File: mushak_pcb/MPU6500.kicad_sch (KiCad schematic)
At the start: 9 parts, among them U5 MPU-6500

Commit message: Add footprints
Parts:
- C31, C32, C33: footprint (none) -> Capacitor_SMD:C_0805_2012Metric
- R16, R17, R18, R19, R20: footprint (none) -> Resistor_SMD:R_0805_2012Metric
- U5: footprint QFN40P300X300X95-25N -> MPU-6500:QFN40P300X300X95-25N
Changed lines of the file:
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@@
     (property "Reference" "R19" (id 0) (at 133.858 54.61 90))
     (property "Value" "10k" (id 1) (at 133.858 57.15 90))
-    (property "Footprint" "" (id 2) (at 133.858 62.484 90)
+    (property "Footprint" "Resistor_SMD:R_0805_2012Metric" (id 2) (at 133.858 62.484 90)
       (effects (font (size 1.27 1.27)) hide)
     )
@@
       (effects (font (size 1.27 1.27)) (justify left))
     )
-    (property "Footprint" "" (id 2) (at 125.73 101.854 90)
+    (property "Footprint" "Resistor_SMD:R_0805_2012Metric" (id 2) (at 125.73 101.854 90)
       (effects (font (size 1.27 1.27)) hide)
     )
@@
     (property "Reference" "R20" (id 0) (at 168.91 85.09 90))
     (property "Value" "10k" (id 1) (at 171.958 82.804 90))
-    (property "Footprint" "" (id 2) (at 171.958 84.582 90)
+    (property "Footprint" "Resistor_SMD:R_0805_2012Metric" (id 2) (at 171.958 84.582 90)
       (effects (font (size 1.27 1.27)) hide)
     )
@@
       (effects (font (size 1.27 1.27)) (justify left))
     )
-    (property "Footprint" "" (id 2) (at 179.2732 54.102 0)
+    (property "Footprint" "Capacitor_SMD:C_0805_2012Metric" (id 2) (at 179.2732 54.102 0)
       (effects (font (size 1.27 1.27)) hide)
     )
@@
       (effects (font (size 1.27 1.27)) (justify left))
     )
-    (property "Footprint" "" (id 2) (at 169.3672 54.102 0)
+    (property "Footprint" "Capacitor_SMD:C_0805_2012Metric" (id 2) (at 169.3672 54.102 0)
       (effects (font (size 1.27 1.27)) hide)
     )
@@
     (property "Reference" "U5" (id 0) (at 148.082 64.77 0))
     (property "Value" "MPU-6500" (id 1) (at 148.082 67.31 0))
-    (property "Footprint" "QFN40P300X300X95-25N" (id 2) (at 148.082 87.884 0)
+    (property "Footprint" "MPU-6500:QFN40P300X300X95-25N" (id 2) (at 148.082 87.884 0)
       (effects (font (size 1.27 1.27)) (justify left bottom) hide)
     )
@@
       (effects (font (size 1.27 1.27)) (justify right))
     )
-    (property "Footprint" "" (id 2) (at 114.3 69.088 90)
+    (property "Footprint" "Resistor_SMD:R_0805_2012Metric" (id 2) (at 114.3 69.088 90)
       (effects (font (size 1.27 1.27)) hide)
     )
@@
     (property "Reference" "C32" (id 0) (at 169.418 88.646 90))
     (property "Value" "0.1uF" (id 1) (at 176.276 88.9 90))
-    (property "Footprint" "" (id 2) (at 168.148 91.3892 0)
+    (property "Footprint" "Capacitor_SMD:C_0805_2012Metric" (id 2) (at 168.148 91.3892 0)
       (effects (font (size 1.27 1.27)) hide)
     )
@@
       (effects (font (size 1.27 1.27)) (justify right))
     )
-    (property "Footprint" "" (id 2) (at 122.428 68.834 90)
-      (effects (font (size 1.27 1.27)) hide)
-    )
+    (property "Footprint" "Resistor_SMD:R_0805_2012Metric" (id 2) (at 122.428 68.834 90)
+      (effects (font (size 1.27 1.27)) hide)
+    )

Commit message: Update Schematics and footprints for sensors
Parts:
- C31, C32, C33: footprint Capacitor_SMD:C_0805_2012Metric -> Capacitor_SMD:C_0402_1005Metric
- R16, R17, R18, R19, R20: footprint Resistor_SMD:R_0805_2012Metric -> Resistor_SMD:R_0402_1005Metric
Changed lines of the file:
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@@
     (property "Reference" "R19" (id 0) (at 133.858 54.61 90))
     (property "Value" "10k" (id 1) (at 133.858 57.15 90))
-    (property "Footprint" "Resistor_SMD:R_0805_2012Metric" (id 2) (at 133.858 62.484 90)
+    (property "Footprint" "Resistor_SMD:R_0402_1005Metric" (id 2) (at 133.858 62.484 90)
       (effects (font (size 1.27 1.27)) hide)
     )
@@
       (effects (font (size 1.27 1.27)) (justify left))
     )
-    (property "Footprint" "Resistor_SMD:R_0805_2012Metric" (id 2) (at 125.73 101.854 90)
+    (property "Footprint" "Resistor_SMD:R_0402_1005Metric" (id 2) (at 125.73 101.854 90)
       (effects (font (size 1.27 1.27)) hide)
     )
@@
     (property "Reference" "R20" (id 0) (at 168.91 85.09 90))
     (property "Value" "10k" (id 1) (at 171.958 82.804 90))
-    (property "Footprint" "Resistor_SMD:R_0805_2012Metric" (id 2) (at 171.958 84.582 90)
+    (property "Footprint" "Resistor_SMD:R_0402_1005Metric" (id 2) (at 171.958 84.582 90)
       (effects (font (size 1.27 1.27)) hide)
     )
@@
       (effects (font (size 1.27 1.27)) (justify left))
     )
-    (property "Footprint" "Capacitor_SMD:C_0805_2012Metric" (id 2) (at 179.2732 54.102 0)
+    (property "Footprint" "Capacitor_SMD:C_0402_1005Metric" (id 2) (at 179.2732 54.102 0)
       (effects (font (size 1.27 1.27)) hide)
     )
@@
       (effects (font (size 1.27 1.27)) (justify left))
     )
-    (property "Footprint" "Capacitor_SMD:C_0805_2012Metric" (id 2) (at 169.3672 54.102 0)
+    (property "Footprint" "Capacitor_SMD:C_0402_1005Metric" (id 2) (at 169.3672 54.102 0)
       (effects (font (size 1.27 1.27)) hide)
     )
@@
       (effects (font (size 1.27 1.27)) (justify left bottom) hide)
     )
-    (property "Datasheet" "" (id 3) (at 148.082 87.884 0)
+    (property "Datasheet" "https://invensense.tdk.com/wp-content/uploads/2020/06/PS-MPU-6500A-01-v1.3.pdf" (id 3) (at 148.082 87.884 0)
       (effects (font (size 1.27 1.27)) (justify left bottom) hide)
     )
@@
       (effects (font (size 1.27 1.27)) (justify right))
     )
-    (property "Footprint" "Resistor_SMD:R_0805_2012Metric" (id 2) (at 114.3 69.088 90)
+    (property "Footprint" "Resistor_SMD:R_0402_1005Metric" (id 2) (at 114.3 69.088 90)
       (effects (font (size 1.27 1.27)) hide)
     )
@@
     (property "Reference" "C32" (id 0) (at 169.418 88.646 90))
     (property "Value" "0.1uF" (id 1) (at 176.276 88.9 90))
-    (property "Footprint" "Capacitor_SMD:C_0805_2012Metric" (id 2) (at 168.148 91.3892 0)
+    (property "Footprint" "Capacitor_SMD:C_0402_1005Metric" (id 2) (at 168.148 91.3892 0)
       (effects (font (size 1.27 1.27)) hide)
     )
@@
       (effects (font (size 1.27 1.27)) (justify right))
     )
-    (property "Footprint" "Resistor_SMD:R_0805_2012Metric" (id 2) (at 122.428 68.834 90)
-      (effects (font (size 1.27 1.27)) hide)
-    )
+    (property "Footprint" "Resistor_SMD:R_0402_1005Metric" (id 2) (at 122.428 68.834 90)
+      (effects (font (size 1.27 1.27)) hide)
+    )

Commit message: changed footprints of capacitors and resistors
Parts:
- C32, C33: footprint Capacitor_SMD:C_0402_1005Metric -> Capacitor_SMD:C_0201_0603Metric
- R16, R17, R18, R19, R20: footprint Resistor_SMD:R_0402_1005Metric -> Resistor_SMD:R_0201_0603Metric
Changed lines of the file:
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@@
     (property "Reference" "R19" (id 0) (at 133.858 54.61 90))
     (property "Value" "10k" (id 1) (at 133.858 57.15 90))
-    (property "Footprint" "Resistor_SMD:R_0402_1005Metric" (id 2) (at 133.858 62.484 90)
+    (property "Footprint" "Resistor_SMD:R_0201_0603Metric" (id 2) (at 133.858 62.484 90)
       (effects (font (size 1.27 1.27)) hide)
     )
@@
       (effects (font (size 1.27 1.27)) (justify left))
     )
-    (property "Footprint" "Resistor_SMD:R_0402_1005Metric" (id 2) (at 125.73 101.854 90)
+    (property "Footprint" "Resistor_SMD:R_0201_0603Metric" (id 2) (at 125.73 101.854 90)
       (effects (font (size 1.27 1.27)) hide)
     )
@@
     (property "Reference" "R20" (id 0) (at 168.91 85.09 90))
     (property "Value" "10k" (id 1) (at 171.958 82.804 90))
-    (property "Footprint" "Resistor_SMD:R_0402_1005Metric" (id 2) (at 171.958 84.582 90)
+    (property "Footprint" "Resistor_SMD:R_0201_0603Metric" (id 2) (at 171.958 84.582 90)
       (effects (font (size 1.27 1.27)) hide)
     )
@@
       (effects (font (size 1.27 1.27)) (justify left))
     )
-    (property "Footprint" "Capacitor_SMD:C_0402_1005Metric" (id 2) (at 179.2732 54.102 0)
+    (property "Footprint" "Capacitor_SMD:C_0201_0603Metric" (id 2) (at 179.2732 54.102 0)
       (effects (font (size 1.27 1.27)) hide)
     )
@@
       (effects (font (size 1.27 1.27)) (justify right))
     )
-    (property "Footprint" "Resistor_SMD:R_0402_1005Metric" (id 2) (at 114.3 69.088 90)
+    (property "Footprint" "Resistor_SMD:R_0201_0603Metric" (id 2) (at 114.3 69.088 90)
       (effects (font (size 1.27 1.27)) hide)
     )
@@
     (property "Reference" "C32" (id 0) (at 169.418 88.646 90))
     (property "Value" "0.1uF" (id 1) (at 176.276 88.9 90))
-    (property "Footprint" "Capacitor_SMD:C_0402_1005Metric" (id 2) (at 168.148 91.3892 0)
+    (property "Footprint" "Capacitor_SMD:C_0201_0603Metric" (id 2) (at 168.148 91.3892 0)
       (effects (font (size 1.27 1.27)) hide)
     )
@@
       (effects (font (size 1.27 1.27)) (justify right))
     )
-    (property "Footprint" "Resistor_SMD:R_0402_1005Metric" (id 2) (at 122.428 68.834 90)
-      (effects (font (size 1.27 1.27)) hide)
-    )
+    (property "Footprint" "Resistor_SMD:R_0201_0603Metric" (id 2) (at 122.428 68.834 90)
+      (effects (font (size 1.27 1.27)) hide)
+    )

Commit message: VL6180x part routed
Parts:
- C31: footprint Capacitor_SMD:C_0402_1005Metric -> Capacitor_SMD:C_0201_0603Metric
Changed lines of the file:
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@@
       (effects (font (size 1.27 1.27)) (justify left))
     )
-    (property "Footprint" "Capacitor_SMD:C_0402_1005Metric" (id 2) (at 169.3672 54.102 0)
+    (property "Footprint" "Capacitor_SMD:C_0201_0603Metric" (id 2) (at 169.3672 54.102 0)
       (effects (font (size 1.27 1.27)) hide)
     )

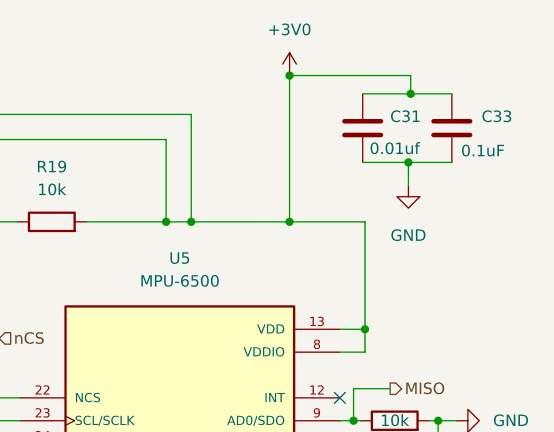
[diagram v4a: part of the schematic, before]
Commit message: changed footprint of passive components
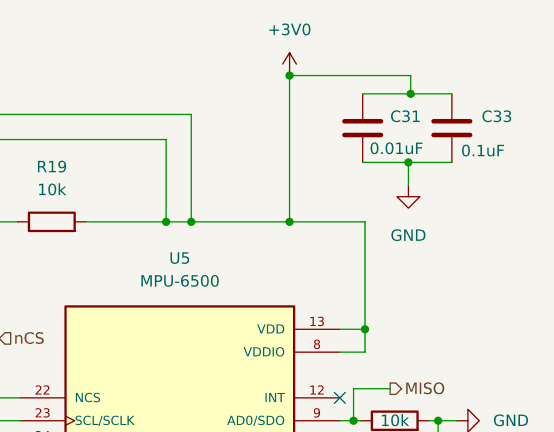
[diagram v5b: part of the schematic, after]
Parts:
- C31: value 0.01uf -> 0.01uF; footprint Capacitor_SMD:C_0201_0603Metric -> Capacitor_SMD:C_0402_1005Metric
- C32, C33: footprint Capacitor_SMD:C_0201_0603Metric -> Capacitor_SMD:C_0402_1005Metric
- R16, R17, R18, R19, R20: footprint Resistor_SMD:R_0201_0603Metric -> Resistor_SMD:R_0402_1005Metric
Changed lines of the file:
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@@
     (property "Reference" "R19" (id 0) (at 133.858 54.61 90))
     (property "Value" "10k" (id 1) (at 133.858 57.15 90))
-    (property "Footprint" "Resistor_SMD:R_0201_0603Metric" (id 2) (at 133.858 62.484 90)
+    (property "Footprint" "Resistor_SMD:R_0402_1005Metric" (id 2) (at 133.858 62.484 90)
       (effects (font (size 1.27 1.27)) hide)
     )
@@
       (effects (font (size 1.27 1.27)) (justify left))
     )
-    (property "Footprint" "Resistor_SMD:R_0201_0603Metric" (id 2) (at 125.73 101.854 90)
+    (property "Footprint" "Resistor_SMD:R_0402_1005Metric" (id 2) (at 125.73 101.854 90)
       (effects (font (size 1.27 1.27)) hide)
     )
@@
     (property "Reference" "R20" (id 0) (at 168.91 85.09 90))
     (property "Value" "10k" (id 1) (at 171.958 82.804 90))
-    (property "Footprint" "Resistor_SMD:R_0201_0603Metric" (id 2) (at 171.958 84.582 90)
+    (property "Footprint" "Resistor_SMD:R_0402_1005Metric" (id 2) (at 171.958 84.582 90)
       (effects (font (size 1.27 1.27)) hide)
     )
@@
       (effects (font (size 1.27 1.27)) (justify left))
     )
-    (property "Footprint" "Capacitor_SMD:C_0201_0603Metric" (id 2) (at 179.2732 54.102 0)
+    (property "Footprint" "Capacitor_SMD:C_0402_1005Metric" (id 2) (at 179.2732 54.102 0)
       (effects (font (size 1.27 1.27)) hide)
     )
@@
       (effects (font (size 1.27 1.27)) (justify left))
     )
-    (property "Value" "0.01uf" (id 1) (at 169.164 52.578 0)
-      (effects (font (size 1.27 1.27)) (justify left))
-    )
-    (property "Footprint" "Capacitor_SMD:C_0201_0603Metric" (id 2) (at 169.3672 54.102 0)
+    (property "Value" "0.01uF" (id 1) (at 169.164 52.578 0)
+      (effects (font (size 1.27 1.27)) (justify left))
+    )
+    (property "Footprint" "Capacitor_SMD:C_0402_1005Metric" (id 2) (at 169.3672 54.102 0)
       (effects (font (size 1.27 1.27)) hide)
     )
@@
       (effects (font (size 1.27 1.27)) (justify right))
     )
-    (property "Footprint" "Resistor_SMD:R_0201_0603Metric" (id 2) (at 114.3 69.088 90)
+    (property "Footprint" "Resistor_SMD:R_0402_1005Metric" (id 2) (at 114.3 69.088 90)
       (effects (font (size 1.27 1.27)) hide)
     )
@@
     (property "Reference" "C32" (id 0) (at 169.418 88.646 90))
     (property "Value" "0.1uF" (id 1) (at 176.276 88.9 90))
-    (property "Footprint" "Capacitor_SMD:C_0201_0603Metric" (id 2) (at 168.148 91.3892 0)
+    (property "Footprint" "Capacitor_SMD:C_0402_1005Metric" (id 2) (at 168.148 91.3892 0)
       (effects (font (size 1.27 1.27)) hide)
     )
@@
       (effects (font (size 1.27 1.27)) (justify right))
     )
-    (property "Footprint" "Resistor_SMD:R_0201_0603Metric" (id 2) (at 122.428 68.834 90)
-      (effects (font (size 1.27 1.27)) hide)
-    )
+    (property "Footprint" "Resistor_SMD:R_0402_1005Metric" (id 2) (at 122.428 68.834 90)
+      (effects (font (size 1.27 1.27)) hide)
+    )

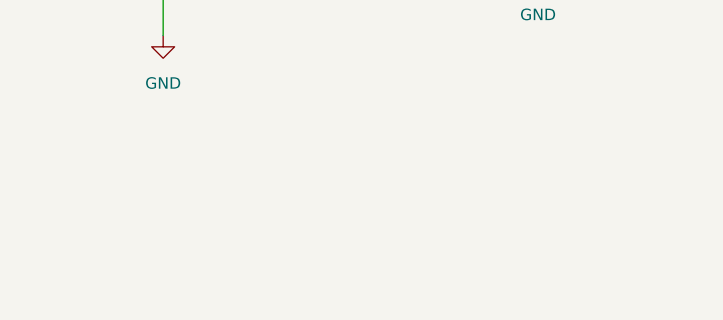
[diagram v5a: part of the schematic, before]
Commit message: changed oscilattor placement
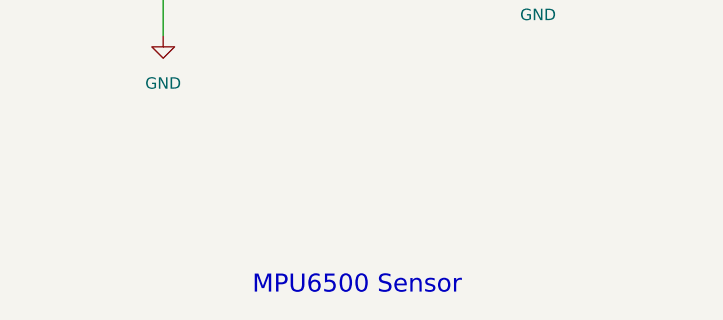
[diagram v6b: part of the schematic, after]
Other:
- note added: "MPU6500 Sensor"
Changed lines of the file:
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@@
     (stroke (width 0) (type default) (color 0 0 0 0))
+  )
+  (text "MPU6500 Sensor" (at 137.414 139.192 0)
+    (effects (font (size 2 2)) (justify left bottom))
   )
   (hierarchical_label "SCLK" (shape input) (at 121.412 81.534 0)
